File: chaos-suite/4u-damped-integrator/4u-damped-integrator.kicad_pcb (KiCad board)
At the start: 2 copper layers, 0 parts

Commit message: Laying out damped integrator pcb
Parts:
- added C1: 100pF, Rumblesan_Footprints:C_Rect_L7.0mm_W3.5mm_P5.00mm, F.Cu at (97.9, 111.0)
- added C10: 100nF, Rumblesan_Footprints:C_Rect_L7.0mm_W3.5mm_P5.00mm, F.Cu at (122.0, 100.6)
- added C11: 1uF, Capacitor_THT:CP_Radial_D5.0mm_P2.00mm, F.Cu at (102.6, 46.7)
- added C12: 1uF, Capacitor_THT:CP_Radial_D5.0mm_P2.00mm, F.Cu at (113.6, 46.7)
- added C2: 1nF, Rumblesan_Footprints:C_Rect_L7.0mm_W3.5mm_P5.00mm, F.Cu at (102.9, 86.6)
- added C3: 100pF, Rumblesan_Footprints:C_Rect_L7.0mm_W3.5mm_P5.00mm, F.Cu at (122.1, 111.0)
- added C4: 1nF, Rumblesan_Footprints:C_Rect_L7.0mm_W3.5mm_P5.00mm, F.Cu at (117.1, 86.6)
- added C5: 100nF, Rumblesan_Footprints:C_Rect_L7.0mm_W3.5mm_P5.00mm, F.Cu at (106.2, 164.6)
- added C6: 100nF, Rumblesan_Footprints:C_Rect_L7.0mm_W3.5mm_P5.00mm, F.Cu at (113.8, 145.1)
- added C7: 100nF, Rumblesan_Footprints:C_Rect_L7.0mm_W3.5mm_P5.00mm, F.Cu at (103.0, 66.0)
- added C8: 100nF, Rumblesan_Footprints:C_Rect_L7.0mm_W3.5mm_P5.00mm, F.Cu at (122.0, 66.0)
- added C9: 100nF, Rumblesan_Footprints:C_Rect_L7.0mm_W3.5mm_P5.00mm, F.Cu at (102.9, 100.6)
- added D1: 1N5818, Rumblesan_Footprints:D_DO-41_SOD81_P10.16mm_Horizontal, F.Cu at (98.0, 46.7)
- added D2: 1N5818, Rumblesan_Footprints:Diode_THT_P10.16mm_Horizontal, F.Cu at (120.1, 36.6)
- added D3: 4v3, Rumblesan_Footprints:D_DO-41_SOD81_P10.16mm_Horizontal, F.Cu at (121.7, 158.0)
- added D4: 4v3, Rumblesan_Footprints:D_DO-41_SOD81_P10.16mm_Horizontal, F.Cu at (121.7, 155.2)
- added H1: MountingHole_Pad, MountingHole:MountingHole_3.2mm_M3_DIN965_Pad, F.Cu at (39.5, 176.5)
- added H10: MouseBite, Panelization:mouse-bite-2mm-slot, F.Cu at (85.0, 75.0)
- added H2: MountingHole_Pad, MountingHole:MountingHole_3.2mm_M3_DIN965_Pad, F.Cu at (80.5, 33.5)
- added H3: MountingHole_Pad, MountingHole:MountingHole_3.2mm_M3_DIN965_Pad, F.Cu at (89.5, 176.5)
- added H4: MountingHole_Pad, MountingHole:MountingHole_3.2mm_M3_DIN965_Pad, F.Cu at (130.5, 33.5)
- added H5: MouseBite, Panelization:mouse-bite-2mm-slot, F.Cu at (85.0, 142.5)
- added H6: MouseBite, Panelization:mouse-bite-2mm-slot, F.Cu at (85.0, 165.0)
- added H7: MouseBite, Panelization:mouse-bite-2mm-slot, F.Cu at (85.0, 120.0)
- added H8: MouseBite, Panelization:mouse-bite-2mm-slot, F.Cu at (85.0, 97.5)
- added H9: MouseBite, Panelization:mouse-bite-2mm-slot, F.Cu at (85.0, 52.5)
- added J1: BananaJack_PanelMount, Rumblesan_Footprints:BananaJack_THT_JohnsonCinch_108-09, B.Cu at (47.3, 75.7)
- added J10: BananaJack_PanelMount, Rumblesan_Footprints:BananaJack_THT_JohnsonCinch_108-09, B.Cu at (72.7, 56.6)
- added J11: BananaJack_PanelMount, Rumblesan_Footprints:BananaJack_THT_JohnsonCinch_108-09, B.Cu at (72.7, 94.8)
- added J12: I2_IO_Ctrl, Connector_PinSocket_2.54mm:PinSocket_1x04_P2.54mm_Vertical, F.Cu at (81.5, 59.0)
- added J13: I2_IO_Main, Connector_PinHeader_2.54mm:PinHeader_1x04_P2.54mm_Vertical, B.Cu at (131.5, 59.0)
- added J14: I2_Damping_Ctrl, Connector_PinSocket_2.54mm:PinSocket_1x02_P2.54mm_Vertical, F.Cu at (81.5, 125.0)
- added J15: I2_Damping_Main, Connector_PinHeader_2.54mm:PinHeader_1x02_P2.54mm_Vertical, B.Cu at (131.5, 125.0)
- added J16: BananaJack_PanelMount, Rumblesan_Footprints:BananaJack_THT_JohnsonCinch_108-09, B.Cu at (72.7, 37.6)
- added J17: 4U_Power, Rumblesan_Footprints:4u_Power_Molex_KK-254_P2.54mm, F.Cu at (105.2, 36.6)
- added J18: BananaJack_PanelMount, Rumblesan_Footprints:BananaJack_THT_JohnsonCinch_108-09, B.Cu at (47.3, 170.9)
- added J19: BananaJack_PanelMount, Rumblesan_Footprints:BananaJack_THT_JohnsonCinch_108-09, B.Cu at (47.3, 151.9)
- added J2: BananaJack_PanelMount, Rumblesan_Footprints:BananaJack_THT_JohnsonCinch_108-09, B.Cu at (47.3, 56.6)
- added J20: BananaJack_PanelMount, Rumblesan_Footprints:BananaJack_THT_JohnsonCinch_108-09, B.Cu at (72.7, 151.9)
- added J21: BananaJack_PanelMount, Rumblesan_Footprints:BananaJack_THT_JohnsonCinch_108-09, B.Cu at (72.7, 170.9)
- added J22: Extras_Ctrl, Connector_PinSocket_2.54mm:PinSocket_1x04_P2.54mm_Vertical, F.Cu at (57.0, 177.0)
- added J23: Extras_Main, Connector_PinHeader_2.54mm:PinHeader_1x04_P2.54mm_Vertical, B.Cu at (107.0, 177.0)
- added J3: BananaJack_PanelMount, Rumblesan_Footprints:BananaJack_THT_JohnsonCinch_108-09, B.Cu at (47.3, 94.8)
- added J4: I1_IO_Ctrl, Connector_PinSocket_2.54mm:PinSocket_1x04_P2.54mm_Vertical, F.Cu at (38.5, 59.0)
- added J5: I1_IO_Main, Connector_PinHeader_2.54mm:PinHeader_1x04_P2.54mm_Vertical, B.Cu at (88.5, 59.0)
- added J6: I1_Damping_Ctrl, Connector_PinSocket_2.54mm:PinSocket_1x04_P2.54mm_Vertical, F.Cu at (38.5, 127.5)
- added J7: I1_Damping_Main, Connector_PinHeader_2.54mm:PinHeader_1x04_P2.54mm_Vertical, B.Cu at (88.5, 127.5)
- added J8: BananaJack_PanelMount, Rumblesan_Footprints:BananaJack_THT_JohnsonCinch_108-09, B.Cu at (47.3, 37.6)
- added J9: BananaJack_PanelMount, Rumblesan_Footprints:BananaJack_THT_JohnsonCinch_108-09, B.Cu at (72.7, 75.7)
- added Q1: 2N3904, Package_TO_SOT_THT:TO-92_Inline_Wide, F.Cu at (99.6, 118.0)
- added Q2: 2N3906, Package_TO_SOT_THT:TO-92_Inline_Wide, F.Cu at (96.0, 120.4)
- added Q3: 2N3904, Package_TO_SOT_THT:TO-92_Inline_Wide, F.Cu at (117.9, 116.8)
- added Q4: 2N3906, Package_TO_SOT_THT:TO-92_Inline_Wide, F.Cu at (123.4, 119.6)
- added R1: 270k, Rumblesan_Footprints:Resistor_THT_L6.3mm_D2.5mm_P10.16mm_Horizontal, F.Cu at (102.9, 97.0)
- added R10: 10k, Rumblesan_Footprints:Resistor_THT_L6.3mm_D2.5mm_P10.16mm_Horizontal, F.Cu at (89.9, 113.5)
- added R11: 270k, Rumblesan_Footprints:Resistor_THT_L6.3mm_D2.5mm_P10.16mm_Horizontal, F.Cu at (108.5, 90.9)
- added R12: 100k, Rumblesan_Footprints:Resistor_THT_L6.3mm_D2.5mm_P10.16mm_Horizontal, F.Cu at (127.3, 73.2)
- added R13: 100k, Rumblesan_Footprints:Resistor_THT_L6.3mm_D2.5mm_P10.16mm_Horizontal, F.Cu at (127.3, 76.2)
- added R14: 100k, Rumblesan_Footprints:Resistor_THT_L6.3mm_D2.5mm_P10.16mm_Horizontal, F.Cu at (127.3, 104.1)
- added R15: 220r, Rumblesan_Footprints:Resistor_THT_L6.3mm_D2.5mm_P10.16mm_Horizontal, F.Cu at (127.3, 70.1)
- added R16: 100k, Rumblesan_Footprints:Resistor_THT_L6.3mm_D2.5mm_P10.16mm_Horizontal, F.Cu at (127.3, 97.0)
- added R17: 220r, Rumblesan_Footprints:Resistor_THT_L6.3mm_D2.5mm_P10.16mm_Horizontal, F.Cu at (127.3, 79.2)
- added R18: 2k, Rumblesan_Footprints:Resistor_THT_L6.3mm_D2.5mm_P10.16mm_Horizontal, F.Cu at (127.3, 107.2)
- added R19: 100k, Rumblesan_Footprints:Resistor_THT_L6.3mm_D2.5mm_P10.16mm_Horizontal, F.Cu at (121.9, 126.0)
- added R2: 100k, Rumblesan_Footprints:Resistor_THT_L6.3mm_D2.5mm_P10.16mm_Horizontal, F.Cu at (92.7, 73.2)
- added R20: 10k, Rumblesan_Footprints:Resistor_THT_L6.3mm_D2.5mm_P10.16mm_Horizontal, F.Cu at (130.0, 113.5)
- added R21: 10k, Rumblesan_Footprints:Resistor_THT_L6.3mm_D2.5mm_P10.16mm_Horizontal, F.Cu at (99.3, 163.1)
- added R22: 10k, Rumblesan_Footprints:Resistor_THT_L6.3mm_D2.5mm_P10.16mm_Horizontal, F.Cu at (102.4, 152.9)
- added R23: 390k, Rumblesan_Footprints:Resistor_THT_L6.3mm_D2.5mm_P10.16mm_Horizontal, F.Cu at (117.9, 157.7)
- added R24: 2k2, Rumblesan_Footprints:Resistor_THT_L6.3mm_D2.5mm_P10.16mm_Horizontal, F.Cu at (128.5, 144.3)
- added R25: 27k, Rumblesan_Footprints:Resistor_THT_L6.3mm_D2.5mm_P10.16mm_Horizontal, F.Cu at (125.2, 144.3)
- added R26: 100k, Rumblesan_Footprints:Resistor_THT_L6.3mm_D2.5mm_P10.16mm_Horizontal, F.Cu at (117.9, 155.4)
- added R27: 100k, Rumblesan_Footprints:Resistor_THT_L6.3mm_D2.5mm_P10.16mm_Horizontal, F.Cu at (125.2, 156.7)
- added R3: 100k, Rumblesan_Footprints:Resistor_THT_L6.3mm_D2.5mm_P10.16mm_Horizontal, F.Cu at (92.7, 76.2)
- added R4: 100k, Rumblesan_Footprints:Resistor_THT_L6.3mm_D2.5mm_P10.16mm_Horizontal, F.Cu at (92.7, 104.1)
- added R5: 220r, Rumblesan_Footprints:Resistor_THT_L6.3mm_D2.5mm_P10.16mm_Horizontal, F.Cu at (92.7, 70.1)
- added R6: 100k, Rumblesan_Footprints:Resistor_THT_L6.3mm_D2.5mm_P10.16mm_Horizontal, F.Cu at (92.7, 94.0)
- added R7: 220r, Rumblesan_Footprints:Resistor_THT_L6.3mm_D2.5mm_P10.16mm_Horizontal, F.Cu at (92.7, 79.2)
- added R8: 2k, Rumblesan_Footprints:Resistor_THT_L6.3mm_D2.5mm_P10.16mm_Horizontal, F.Cu at (92.7, 107.2)
- added R9: 100k, Rumblesan_Footprints:Resistor_THT_L6.3mm_D2.5mm_P10.16mm_Horizontal, F.Cu at (101.6, 122.7)
- added RV1: 100k, Rumblesan_Footprints:Potentiometer_Alpha_RD901F-40-00D_Single_Vertical_CircularHoles, B.Cu at (47.3, 132.8)
- added RV2: 100k, Rumblesan_Footprints:Potentiometer_Alpha_RD901F-40-00D_Single_Vertical_CircularHoles, B.Cu at (47.3, 113.8)
- added RV3: 100k, Rumblesan_Footprints:Potentiometer_Alpha_RD901F-40-00D_Single_Vertical_CircularHoles, B.Cu at (72.7, 132.8)
- added RV4: 100k, Rumblesan_Footprints:Potentiometer_Alpha_RD901F-40-00D_Single_Vertical_CircularHoles, B.Cu at (72.7, 113.8)
- added U1: TL074, Rumblesan_Footprints:DIP-14_W7.62mm_Socket, F.Cu at (113.8, 109.5)
- added U2: LM13700, Rumblesan_Footprints:DIP-16_W7.62mm_Socket, F.Cu at (113.8, 79.8)
- added U3: TL072, Rumblesan_Footprints:DIP-8_W7.62mm_Socket, F.Cu at (113.8, 160.8)
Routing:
- net +12V: track 0.00 -> 214.5 mm
- net -12V: track 0.00 -> 122.2 mm
- net /I2_Output_Main: track 0.00 -> 48.7 mm
- net /I1_Output_Main: track 0.00 -> 48.0 mm
- net Net-(C1-Pad1): track 0.00 -> 43.4 mm
- net Net-(C3-Pad1): track 0.00 -> 35.4 mm
- net Net-(C2-Pad1): track 0.00 -> 34.7 mm
- net Net-(U2-Pad5): track 0.00 -> 34.7 mm
- net /Extras/Inverter_Output_Ctrl: track 0.00 -> 34.5 mm
- net /Extras/NonLinearity_Input_Ctrl: track 0.00 -> 33.8 mm
- net Net-(U2-Pad1): track 0.00 -> 32.4 mm
- net Net-(R10-Pad2): track 0.00 -> 32.3 mm
- net Net-(J11-Pad1): track 0.00 -> 31.9 mm
- net Net-(J3-Pad1): track 0.00 -> 31.9 mm
- net /I1_DampingCV_Main: track 0.00 -> 31.4 mm
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- added copper zone on B.Cu, net GND
- added copper zone on F.Cu, net GND
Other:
- board outline added: 98 x 150 mm
- net class Default removed
- net class Power removed
- net class Signal removed
- board text added: "Damped Integrator revision 01"
- board text added: "This side towards panel"

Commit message: final damped integrator tweaks
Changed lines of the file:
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@@
   (title_block
     (title "Damped Integrator and extras")
-    (date "2022-05-21")
+    (date "2022-06-17")
     (rev "r01")
+    (comment 2 "creativecommons.org/licenses/by/4.0/")
+    (comment 3 "License: CC BY 4.0")
+    (comment 4 "Author: Guy John")
   )
   (layers
@@
       (drillshape 0)
       (scaleselection 1)
-      (outputdirectory "")
+      (outputdirectory "pcb-gerbers/")
     )
   )
@@
   (net 58 "unconnected-(U2-Pad15)")
   (net 59 "unconnected-(U2-Pad8)")
-  (net 60 "Net-(U2-Pad5)")
+  (net 60 "Net-(C4-Pad1)")
   (net 61 "Net-(R2-Pad2)")
-  (net 62 "Net-(U2-Pad1)")
+  (net 62 "Net-(R20-Pad2)")
   (footprint "Rumblesan_Footprints:Resistor_THT_L6.3mm_D2.5mm_P10.16mm_Horizontal" (layer "F.Cu")
     (at 99.314 163.068 90)
@@
     (fp_line (start 1.635 -1.27) (end 6.985 -1.27) (layer "F.Fab") (width 0.1))
     (pad "1" thru_hole rect locked (at 0 0 180) (size 1.6 1.6) (drill 0.8) (layers *.Cu *.Mask)
-      (net 62 "Net-(U2-Pad1)") (pintype "input"))
+      (net 62 "Net-(R20-Pad2)") (pintype "input"))
     (pad "2" thru_hole oval locked (at 0 2.54 180) (size 1.6 1.6) (drill 0.8) (layers *.Cu *.Mask)
       (net 55 "unconnected-(U2-Pad2)") (pinfunction "DIODE_BIAS") (pintype "input+no_connect"))
@@
       (net 49 "Net-(R12-Pad2)") (pinfunction "-") (pintype "input"))
     (pad "5" thru_hole oval locked (at 0 10.16 180) (size 1.6 1.6) (drill 0.8) (layers *.Cu *.Mask)
-      (net 60 "Net-(U2-Pad5)") (pintype "output"))
+      (net 60 "Net-(C4-Pad1)") (pintype "output"))
     (pad "6" thru_hole oval locked (at 0 12.7 180) (size 1.6 1.6) (drill 0.8) (layers *.Cu *.Mask)
       (net 10 "-12V") (pinfunction "V-") (pintype "power_in"))
@@
     (fp_line (start -1.27 -0.5) (end -0.562893 0) (layer "F.Fab") (width 0.1))
     (fp_line (start 8.89 -2.92) (end -1.27 -2.92) (layer "F.Fab") (width 0.1))
-    (pad "1" thru_hole roundrect (at 0 0) (size 1.74 2.19) (drill 1.19) (layers *.Cu *.Mask) (roundrect_rratio 0.143678)
+    (pad "1" thru_hole roundrect (at 0 0) (size 1.74 2.19) (drill 1.19) (layers *.Cu *.Mask) (roundrect_rratio 0.1436781609)
       (net 11 "Net-(D1-Pad2)") (pinfunction "+12V") (pintype "power_out"))
     (pad "2" thru_hole oval (at 2.54 0) (size 1.74 2.19) (drill 1.19) (layers *.Cu *.Mask)
@@
       (net 46 "Net-(Q4-Pad3)") (pintype "passive"))
     (pad "2" thru_hole oval (at 10.16 0 90) (size 1.6 1.6) (drill 0.8) (layers *.Cu *.Mask)
-      (net 62 "Net-(U2-Pad1)") (pintype "passive"))
+      (net 62 "Net-(R20-Pad2)") (pintype "passive"))
     (model "${KISYS3DMOD}/Resistor_THT.3dshapes/R_Axial_DIN0207_L6.3mm_D2.5mm_P10.16mm_Horizontal.wrl"
       (offset (xyz 0 0 0))
@@
     (fp_line (start -1 1.75) (end 6 1.75) (layer "F.Fab") (width 0.1))
     (pad "1" thru_hole circle (at 0 0) (size 1.6 1.6) (drill 0.8) (layers *.Cu *.Mask)
-      (net 60 "Net-(U2-Pad5)") (pintype "passive"))
+      (net 60 "Net-(C4-Pad1)") (pintype "passive"))
     (pad "2" thru_hole circle (at 5 0) (size 1.6 1.6) (drill 0.8) (layers *.Cu *.Mask)
       (net 7 "/I2_Output_Main") (pintype "passive"))
@@
       (net 9 "GND") (pinfunction "+") (pintype "input"))
     (pad "6" thru_hole oval locked (at 0 12.7 180) (size 1.6 1.6) (drill 0.8) (layers *.Cu *.Mask)
-      (net 60 "Net-(U2-Pad5)") (pinfunction "-") (pintype "input"))
+      (net 60 "Net-(C4-Pad1)") (pinfunction "-") (pintype "input"))
     (pad "7" thru_hole oval locked (at 0 15.24 180) (size 1.6 1.6) (drill 0.8) (layers *.Cu *.Mask)
       (net 7 "/I2_Output_Main") (pintype "output"))

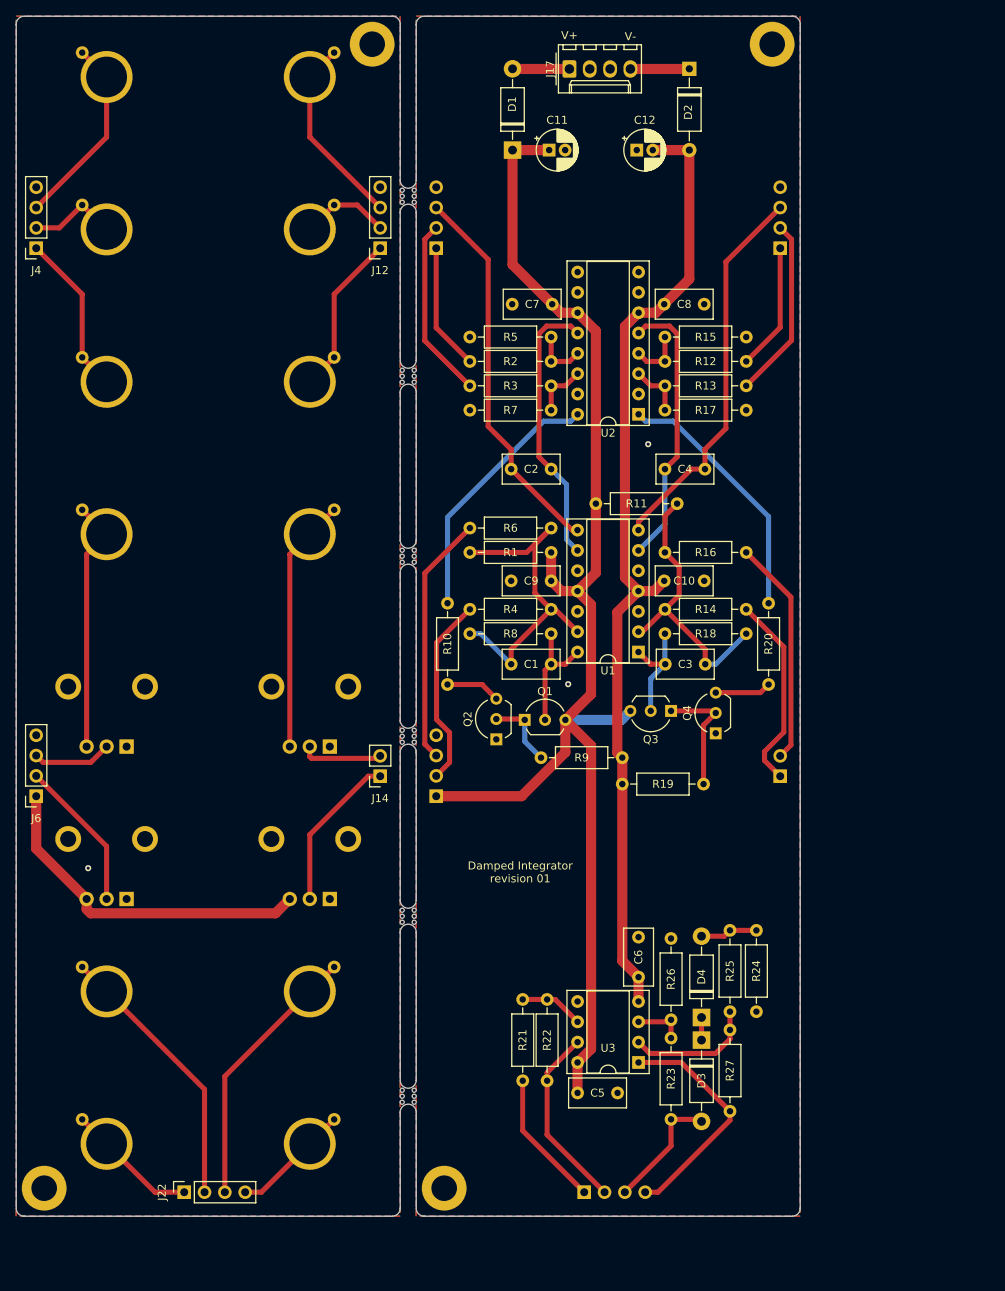
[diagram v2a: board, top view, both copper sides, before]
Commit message: Updating damped integrator circuit and layout
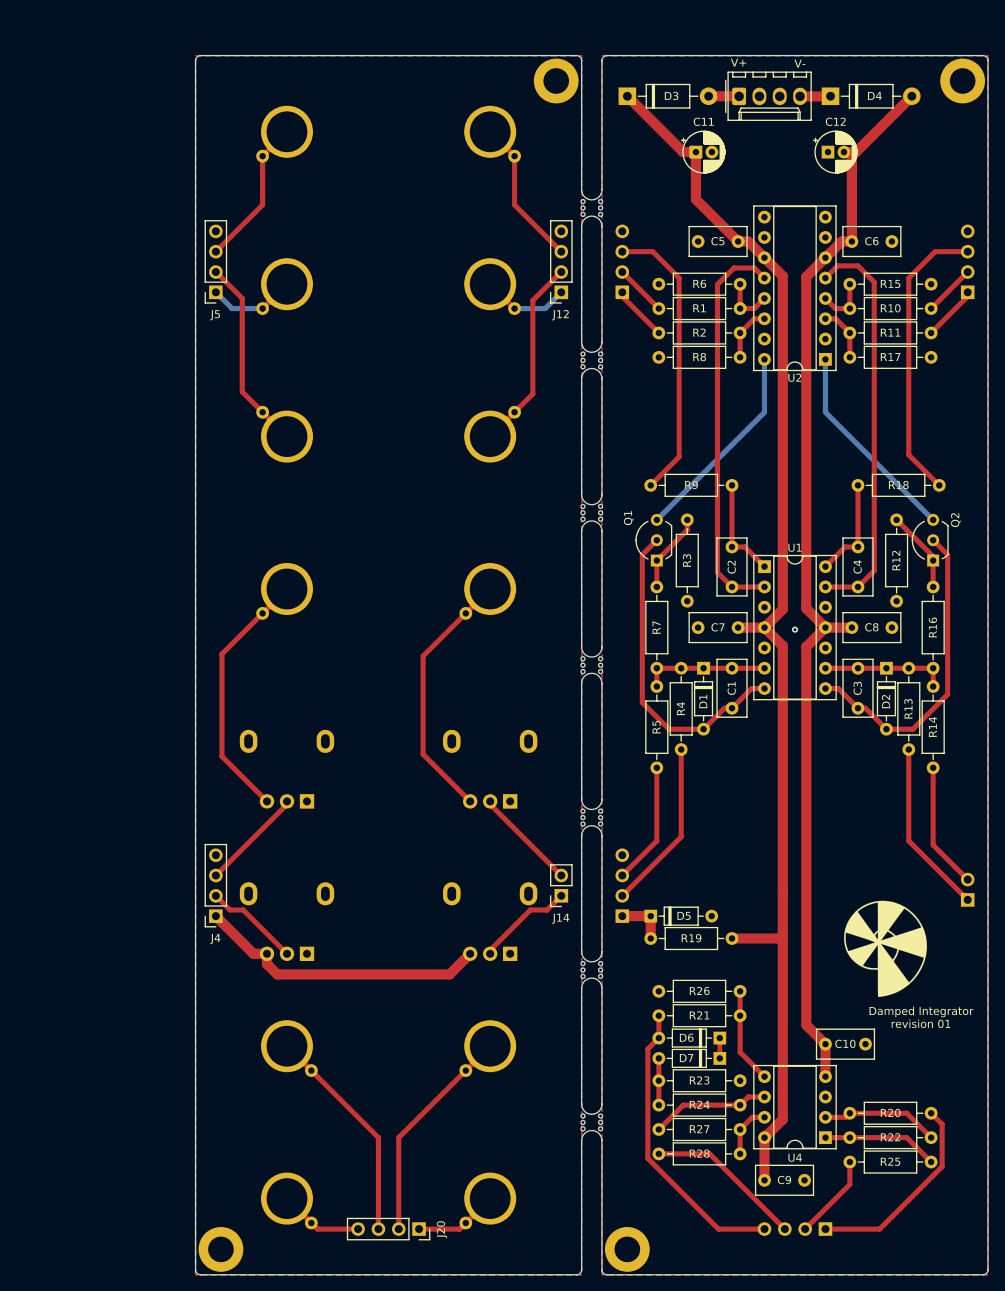
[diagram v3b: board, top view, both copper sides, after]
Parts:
- removed H10, H5, H6, H7, H8, H9: MouseBite, Panelization:mouse-bite-2mm-slot
- removed Q3: 2N3904, Package_TO_SOT_THT:TO-92_Inline_Wide
- removed Q4: 2N3906, Package_TO_SOT_THT:TO-92_Inline_Wide
- removed U3: TL072, Rumblesan_Footprints:DIP-8_W7.62mm_Socket
- added D5: 5v1, rumblesan-standard-parts:D_DO-35_SOD27_P7.62mm_Horizontal, F.Cu at (115.3, 142.5)
- added D6: 4v3, rumblesan-standard-parts:D_DO-35_SOD27_P7.62mm_Horizontal, F.Cu at (124.0, 157.7)
- added D7: 4v3, rumblesan-standard-parts:D_DO-35_SOD27_P7.62mm_Horizontal, F.Cu at (124.0, 160.3)
- added G***: LOGO, Rumblesan_Panel_Graphics:Logo_Ammonite-simple_small_10.4mmx12.0mm, F.Cu at (144.0, 145.5)
- added R28: 330r, rumblesan-standard-parts:R_Axial_DIN0207_L6.3mm_D2.5mm_P10.16mm_Horizontal, F.Cu at (116.3, 172.2)
- added U4: TL072, rumblesan-standard-parts:DIP-8_W7.62mm_Socket, F.Cu at (137.2, 170.2)
- added mouse-bite-2.54mm-slot: VAL**, Panelization:mouse-bite-2.54mm-slot, F.Cu at (108.0, 92.1)
- added mouse-bite-2.54mm-slot: VAL**, Panelization:mouse-bite-2.54mm-slot, F.Cu at (108.0, 73.0)
- added mouse-bite-2.54mm-slot: VAL**, Panelization:mouse-bite-2.54mm-slot, F.Cu at (108.0, 54.0)
- added mouse-bite-2.54mm-slot: VAL**, Panelization:mouse-bite-2.54mm-slot, F.Cu at (108.0, 130.2)
- added mouse-bite-2.54mm-slot: VAL**, Panelization:mouse-bite-2.54mm-slot, F.Cu at (108.0, 149.2)
- added mouse-bite-2.54mm-slot: VAL**, Panelization:mouse-bite-2.54mm-slot, F.Cu at (108.0, 111.1)
- added mouse-bite-2.54mm-slot: VAL**, Panelization:mouse-bite-2.54mm-slot, F.Cu at (108.0, 168.3)
- C1, C10, C2, C3, C4, C5, C6, C7, C8, C9: footprint Rumblesan_Footprints:C_Rect_L7.0mm_W3.5mm_P5.00mm -> rumblesan-standard-parts:C_Rect_L7.0mm_W3.5mm_P5.00mm
- C11, C12: footprint Capacitor_THT:CP_Radial_D5.0mm_P2.00mm -> rumblesan-standard-parts:CP_Radial_D5.0mm_P2.00mm
- D1: value 1N5818 -> 1n4148; footprint Rumblesan_Footprints:D_DO-41_SOD81_P10.16mm_Horizontal -> rumblesan-standard-parts:D_DO-35_SOD27_P7.62mm_Horizontal
- D2: value 1N5818 -> 1n4148; footprint Rumblesan_Footprints:Diode_THT_P10.16mm_Horizontal -> rumblesan-standard-parts:D_DO-35_SOD27_P7.62mm_Horizontal
- D3, D4: value 4v3 -> 1N5818; footprint Rumblesan_Footprints:D_DO-41_SOD81_P10.16mm_Horizontal -> rumblesan-standard-parts:D_DO-41_SOD81_P10.16mm_Horizontal
- H1, H2, H3, H4: footprint MountingHole:MountingHole_3.2mm_M3_DIN965_Pad -> rumblesan-standard-parts:MountingHole_3.2mm_M3_DIN965_Pad
- J1, J10, J11, J16, J18, J19, J2, J3, J8, J9: value BananaJack_PanelMount -> Banana Socket PanelMount; footprint Rumblesan_Footprints:BananaJack_THT_JohnsonCinch_108-09 -> rumblesan-standard-parts:BananaJack_THT_JohnsonCinch_108-09
- J12: value I2_IO_Ctrl -> Conn_01x04_Female
- J13: value I2_IO_Main -> Conn_01x04_Male
- J14: value I2_Damping_Ctrl -> Conn_01x02_Female
- J15: value I2_Damping_Main -> Conn_01x02_Male
- J17: footprint Rumblesan_Footprints:4u_Power_Molex_KK-254_P2.54mm -> 4u-power:4u_Power_Molex_KK-254_P2.54mm
- J20: value BananaJack_PanelMount -> Conn_01x04_Female; footprint Rumblesan_Footprints:BananaJack_THT_JohnsonCinch_108-09 -> Connector_PinSocket_2.54mm:PinSocket_1x04_P2.54mm_Vertical; moved to F.Cu
- J21: value BananaJack_PanelMount -> Conn_01x04_Male; footprint Rumblesan_Footprints:BananaJack_THT_JohnsonCinch_108-09 -> Connector_PinHeader_2.54mm:PinHeader_1x04_P2.54mm_Vertical
- J22: value Extras_Ctrl -> Banana Socket PanelMount; footprint Connector_PinSocket_2.54mm:PinSocket_1x04_P2.54mm_Vertical -> rumblesan-standard-parts:BananaJack_THT_JohnsonCinch_108-09; moved to B.Cu
- J23: value Extras_Main -> Banana Socket PanelMount; footprint Connector_PinHeader_2.54mm:PinHeader_1x04_P2.54mm_Vertical -> rumblesan-standard-parts:BananaJack_THT_JohnsonCinch_108-09
- J4: value I1_IO_Ctrl -> Conn_01x04_Female
- J5: value I1_IO_Main -> Conn_01x04_Female; footprint Connector_PinHeader_2.54mm:PinHeader_1x04_P2.54mm_Vertical -> Connector_PinSocket_2.54mm:PinSocket_1x04_P2.54mm_Vertical; moved to F.Cu
- J6: value I1_Damping_Ctrl -> Conn_01x04_Male; footprint Connector_PinSocket_2.54mm:PinSocket_1x04_P2.54mm_Vertical -> Connector_PinHeader_2.54mm:PinHeader_1x04_P2.54mm_Vertical; moved to B.Cu
- J7: value I1_Damping_Main -> Conn_01x04_Male
- Q1: value 2N3904 -> 2N3906
- R1, R11: value 270k -> 100k; footprint Rumblesan_Footprints:Resistor_THT_L6.3mm_D2.5mm_P10.16mm_Horizontal -> rumblesan-standard-parts:R_Axial_DIN0207_L6.3mm_D2.5mm_P10.16mm_Horizontal
- R10: value 10k -> 100k; footprint Rumblesan_Footprints:Resistor_THT_L6.3mm_D2.5mm_P10.16mm_Horizontal -> rumblesan-standard-parts:R_Axial_DIN0207_L6.3mm_D2.5mm_P10.16mm_Horizontal
- R12, R3: value 100k -> 10k; footprint Rumblesan_Footprints:Resistor_THT_L6.3mm_D2.5mm_P10.16mm_Horizontal -> rumblesan-standard-parts:R_Axial_DIN0207_L6.3mm_D2.5mm_P10.16mm_Horizontal
- R13, R14, R15, R16, R17, R2, R20, R22, R26, R27, R4: footprint Rumblesan_Footprints:Resistor_THT_L6.3mm_D2.5mm_P10.16mm_Horizontal -> rumblesan-standard-parts:R_Axial_DIN0207_L6.3mm_D2.5mm_P10.16mm_Horizontal
- R18: value 2k -> 330r; footprint Rumblesan_Footprints:Resistor_THT_L6.3mm_D2.5mm_P10.16mm_Horizontal -> rumblesan-standard-parts:R_Axial_DIN0207_L6.3mm_D2.5mm_P10.16mm_Horizontal
- R19: value 100k -> 1k; footprint Rumblesan_Footprints:Resistor_THT_L6.3mm_D2.5mm_P10.16mm_Horizontal -> rumblesan-standard-parts:R_Axial_DIN0207_L6.3mm_D2.5mm_P10.16mm_Horizontal
- R21: value 10k -> 390k; footprint Rumblesan_Footprints:Resistor_THT_L6.3mm_D2.5mm_P10.16mm_Horizontal -> rumblesan-standard-parts:R_Axial_DIN0207_L6.3mm_D2.5mm_P10.16mm_Horizontal
- R23: value 390k -> 2k2; footprint Rumblesan_Footprints:Resistor_THT_L6.3mm_D2.5mm_P10.16mm_Horizontal -> rumblesan-standard-parts:R_Axial_DIN0207_L6.3mm_D2.5mm_P10.16mm_Horizontal
- R24: value 2k2 -> 27k; footprint Rumblesan_Footprints:Resistor_THT_L6.3mm_D2.5mm_P10.16mm_Horizontal -> rumblesan-standard-parts:R_Axial_DIN0207_L6.3mm_D2.5mm_P10.16mm_Horizontal
- R25: value 27k -> 330r; footprint Rumblesan_Footprints:Resistor_THT_L6.3mm_D2.5mm_P10.16mm_Horizontal -> rumblesan-standard-parts:R_Axial_DIN0207_L6.3mm_D2.5mm_P10.16mm_Horizontal
- R5, R7: value 220r -> 100k; footprint Rumblesan_Footprints:Resistor_THT_L6.3mm_D2.5mm_P10.16mm_Horizontal -> rumblesan-standard-parts:R_Axial_DIN0207_L6.3mm_D2.5mm_P10.16mm_Horizontal
- R6: value 100k -> 220r; footprint Rumblesan_Footprints:Resistor_THT_L6.3mm_D2.5mm_P10.16mm_Horizontal -> rumblesan-standard-parts:R_Axial_DIN0207_L6.3mm_D2.5mm_P10.16mm_Horizontal
- R8: value 2k -> 220r; footprint Rumblesan_Footprints:Resistor_THT_L6.3mm_D2.5mm_P10.16mm_Horizontal -> rumblesan-standard-parts:R_Axial_DIN0207_L6.3mm_D2.5mm_P10.16mm_Horizontal
- R9: value 100k -> 330r; footprint Rumblesan_Footprints:Resistor_THT_L6.3mm_D2.5mm_P10.16mm_Horizontal -> rumblesan-standard-parts:R_Axial_DIN0207_L6.3mm_D2.5mm_P10.16mm_Horizontal
- RV1, RV2, RV3, RV4: footprint Rumblesan_Footprints:Potentiometer_Alpha_RD901F-40-00D_Single_Vertical_CircularHoles -> rumblesan-standard-parts:Potentiometer_Alpha_RD901F-40-00D_Single_Vertical
- U1: footprint Rumblesan_Footprints:DIP-14_W7.62mm_Socket -> rumblesan-standard-parts:DIP-14_W7.62mm_Socket
- U2: footprint Rumblesan_Footprints:DIP-16_W7.62mm_Socket -> rumblesan-standard-parts:DIP-16_W7.62mm_Socket
- moved D3 118.3 mm to (112.4, 40.0), turned to 0 degrees
- moved D4 116.3 mm to (137.8, 40.0), turned to 0 degrees
- moved C5 108.3 mm to (126.2, 58.2), turned to 180 degrees
- moved C6 92.5 mm to (145.5, 58.2), turned to 180 degrees
- moved J4 86.5 mm to (61.0, 142.5)
- moved C9 79.5 mm to (129.5, 175.5), turned to 0 degrees
- moved D2 78.9 mm to (144.8, 111.5)
- moved J6 74.8 mm to (111.8, 142.5), turned to 0 degrees
- moved D1 69.0 mm to (121.9, 111.5), turned to -90 degrees
- moved R10 68.8 mm to (140.2, 66.5), turned to 0 degrees
- moved J7 67.1 mm to (111.8, 64.5)
- moved J21 65.3 mm to (137.2, 181.6)
- moved C10 61.3 mm to (142.2, 158.5)
- moved Q2 59.0 mm to (150.6, 98.0)
- moved R5 58.7 mm to (116.1, 124.0), turned to 90 degrees
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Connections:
- C2 pad 2: /I1_Output_Main -> Net-(C2-Pad2)
- C4 pad 2: /I2_Output_Main -> Net-(C4-Pad2)
- D1 pad 1: +12V -> Net-(C1-Pad1)
- D1 pad 2: Net-(D1-Pad2) -> Net-(C1-Pad2)
- D2 pad 1: Net-(D2-Pad1) -> Net-(C3-Pad1)
- D2 pad 2: -12V -> Net-(C3-Pad2)
- D3 pad 1: Net-(D3-Pad1) -> +12V
- D3 pad 2: /Extras/NonLinearity_Input_Main -> Net-(D3-Pad2)
- D4 pad 1: Net-(D3-Pad1) -> Net-(D4-Pad1)
- D4 pad 2: Net-(D4-Pad2) -> -12V
- J10 pad 1: /I2_InputPos_Ctrl -> /I2_InputNeg_Ctrl
- J11 pad 1: Net-(J11-Pad1) -> /I2_InputPos_Ctrl
- J12 pad 1: /I2_InputNeg_Ctrl -> /I2_InputPos_Ctrl
- J12 pad 2: /I2_InputPos_Ctrl -> /I2_InputNeg_Ctrl
- J13 pad 1: /I2_InputNeg_Main -> /I2_InputPos_Main
- J13 pad 2: /I2_InputPos_Main -> /I2_InputNeg_Main
- J14 pad 1: /I2_Damping_Ctrl -> /I2_Rate_Ctrl
- J14 pad 2: /I2_DampingCV_Ctrl -> /I2_RateCV_Ctrl
- J15 pad 1: /I2_Damping_Main -> /I2_Rate_Main
- J15 pad 2: /I2_DampingCV_Main -> /I2_RateCV_Main
- J17 pad 1: Net-(D1-Pad2) -> Net-(D3-Pad2)
- J17 pad 4: Net-(D2-Pad1) -> Net-(D4-Pad1)
- J19 pad 1: /Extras/Inverter_Output_Ctrl -> /Extras/NonLinearity_Input_Ctrl
- J20 pad 1: /Extras/NonLinearity_Input_Ctrl -> /Extras/Inverter_Input_Ctrl
- J21 pad 1: /Extras/NonLinearity_Output_Ctrl -> /Extras/Inverter_Input_Main
- J22 pad 1: /Extras/Inverter_Input_Ctrl -> /Extras/Inverter_Output_Ctrl
- J23 pad 1: /Extras/Inverter_Input_Main -> /Extras/NonLinearity_Output_Ctrl
- J4 pad 1: /I1_InputNeg_Ctrl -> V_REF
- J4 pad 2: /I1_InputPos_Ctrl -> /I1_Rate_Ctrl
- J4 pad 3: /I1_Output_Ctrl -> /I1_RateCV_Ctrl
- J5 pad 1: /I1_InputNeg_Main -> /I1_InputPos_Ctrl
- J5 pad 2: /I1_InputPos_Main -> /I1_InputNeg_Ctrl
- J5 pad 3: /I1_Output_Main -> /I1_Output_Ctrl
- J6 pad 1: +12V -> V_REF
- J6 pad 2: /I1_Damping_Ctrl -> /I1_Rate_Main
- J6 pad 3: /I1_DampingCV_Ctrl -> /I1_RateCV_Main
- J7 pad 1: +12V -> /I1_InputPos_Main
- J7 pad 2: /I1_Damping_Main -> /I1_InputNeg_Main
- J7 pad 3: /I1_DampingCV_Main -> /I1_Output_Main
- J9 pad 1: /I2_InputNeg_Ctrl -> Net-(J9-Pad1)
- Q1 pad 3: +12V -> Net-(Q1-Pad3)
- Q2 pad 1: GND -> Net-(Q2-Pad1)
- Q2 pad 2: Net-(Q1-Pad1) -> Net-(C3-Pad2)
- R1 pad 1: +12V -> Net-(R1-Pad1)
- R1 pad 2: Net-(C1-Pad1) -> /I1_InputNeg_Main
- R10 pad 1: Net-(Q2-Pad3) -> Net-(R10-Pad1)
- R10 pad 2: Net-(R10-Pad2) -> /I2_InputNeg_Main
- R11 pad 1: +12V -> Net-(R11-Pad1)
- R11 pad 2: Net-(C3-Pad1) -> /I2_InputPos_Main
- R12 pad 1: /I2_InputNeg_Main -> GND
- R12 pad 2: Net-(R12-Pad2) -> Net-(Q2-Pad1)
- R13 pad 1: /I2_InputPos_Main -> Net-(C3-Pad1)
- R13 pad 2: Net-(R13-Pad2) -> /I2_Rate_Main
- R14 pad 1: /I2_Damping_Main -> /I2_RateCV_Main
- R15 pad 1: GND -> Net-(R10-Pad1)
- R15 pad 2: Net-(R12-Pad2) -> GND
- R16 pad 1: /I2_DampingCV_Main -> Net-(Q2-Pad1)
- R17 pad 1: GND -> Net-(R11-Pad1)
- R17 pad 2: Net-(R13-Pad2) -> GND
- R18 pad 1: Net-(C3-Pad1) -> /I2_Output_Main
- R18 pad 2: Net-(C3-Pad2) -> Net-(C4-Pad2)
- R19 pad 1: Net-(Q3-Pad1) -> V_REF
- R19 pad 2: -12V -> +12V
- R2 pad 1: /I1_InputNeg_Main -> Net-(R2-Pad1)
- R2 pad 2: Net-(R2-Pad2) -> /I1_InputPos_Main
- R20 pad 1: Net-(Q4-Pad3) -> Net-(R20-Pad1)
- R20 pad 2: Net-(R20-Pad2) -> /Extras/Inverter_Input_Main
- R21 pad 1: /Extras/Inverter_Input_Main -> /Extras/NonLinearity_Input_Main
- R22 pad 1: Net-(R21-Pad2) -> Net-(R22-Pad1)
- R22 pad 2: /Extras/Inverter_Output_Main -> Net-(R20-Pad1)
- R23 pad 1: Net-(R23-Pad1) -> GND
- R23 pad 2: /Extras/NonLinearity_Input_Main -> Net-(D7-Pad2)
- R24 pad 1: Net-(D4-Pad2) -> Net-(R24-Pad1)
- R24 pad 2: GND -> Net-(D7-Pad2)
- R25 pad 1: Net-(D4-Pad2) -> /Extras/Inverter_Output_Main
- R25 pad 2: Net-(R25-Pad2) -> Net-(R22-Pad1)
- R26 pad 1: Net-(R23-Pad1) -> GND
- R26 pad 2: GND -> Net-(R21-Pad2)
- R27 pad 1: Net-(R25-Pad2) -> Net-(R27-Pad1)
- R27 pad 2: /Extras/NonLinearity_Output_Main -> Net-(R24-Pad1)
- R3 pad 1: /I1_InputPos_Main -> GND
- R3 pad 2: Net-(R3-Pad2) -> Net-(Q1-Pad1)
- R4 pad 1: /I1_Damping_Main -> Net-(C1-Pad1)
- R4 pad 2: Net-(C1-Pad1) -> /I1_Rate_Main
- R5 pad 1: GND -> /I1_RateCV_Main
- R5 pad 2: Net-(R2-Pad2) -> Net-(C1-Pad1)
- R6 pad 1: /I1_DampingCV_Main -> Net-(R1-Pad1)
- R6 pad 2: Net-(C1-Pad1) -> GND
- R7 pad 1: GND -> Net-(Q1-Pad1)
- R7 pad 2: Net-(R3-Pad2) -> Net-(C1-Pad1)
- R8 pad 1: Net-(C1-Pad1) -> Net-(R2-Pad1)
- R8 pad 2: Net-(C1-Pad2) -> GND
- R9 pad 1: Net-(Q1-Pad1) -> /I1_Output_Main
- R9 pad 2: -12V -> Net-(C2-Pad2)
- RV1 pad 2: /I1_Damping_Ctrl -> /I1_RateCV_Ctrl
- RV1 pad 3: +12V -> Net-(J3-Pad1)
- RV2 pad 2: /I1_DampingCV_Ctrl -> /I1_Rate_Ctrl
- RV2 pad 3: Net-(J3-Pad1) -> V_REF
- RV3 pad 2: /I2_Damping_Ctrl -> /I2_RateCV_Ctrl
- RV3 pad 3: +12V -> Net-(J9-Pad1)
- RV4 pad 2: /I2_DampingCV_Ctrl -> /I2_Rate_Ctrl
- RV4 pad 3: Net-(J11-Pad1) -> V_REF
- U1 pad 1: Net-(C3-Pad2) -> Net-(C2-Pad2)
- U1 pad 11: +12V -> -12V
- U1 pad 13: Net-(C1-Pad1) -> Net-(C4-Pad1)
- U1 pad 14: Net-(C1-Pad2) -> Net-(C4-Pad2)
- U1 pad 2: Net-(C3-Pad1) -> Net-(C2-Pad1)
- U1 pad 4: -12V -> +12V
- U1 pad 6: Net-(C4-Pad1) -> Net-(C1-Pad1)
- U1 pad 7: /I2_Output_Main -> Net-(C1-Pad2)
- U1 pad 8: /I1_Output_Main -> Net-(C3-Pad2)
- U1 pad 9: Net-(C2-Pad1) -> Net-(C3-Pad1)
- U2 pad 1: Net-(R20-Pad2) -> Net-(Q2-Pad3)
- U2 pad 13: Net-(R2-Pad2) -> Net-(R1-Pad1)
- U2 pad 14: Net-(R3-Pad2) -> Net-(R2-Pad1)
- U2 pad 16: Net-(R10-Pad2) -> Net-(Q1-Pad3)
- U2 pad 3: Net-(R13-Pad2) -> Net-(R11-Pad1)
- U2 pad 4: Net-(R12-Pad2) -> Net-(R10-Pad1)
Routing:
- net +12V: track 214.5 -> 157.8 mm
- net V_REF: track 0.00 -> 43.0 mm
- net Net-(J9-Pad1): track 0.00 -> 32.5 mm
- net Net-(R20-Pad2): track 32.4 -> 0.00 mm
- net Net-(R10-Pad2): track 32.3 -> 0.00 mm
- net Net-(J11-Pad1): track 31.9 -> 0.00 mm
- net /I1_DampingCV_Main: track 31.4 -> 0.00 mm
- net /I2_DampingCV_Main: track 28.3 -> 0.00 mm
- net Net-(C1-Pad1): track 43.4 -> 15.7 mm
- net Net-(Q1-Pad3): track 0.00 -> 25.6 mm
- net Net-(C3-Pad2): track 14.3 -> 39.2 mm
- net Net-(C1-Pad2): track 15.0 -> 39.8 mm
- net /I2_Damping_Main: track 24.6 -> 0.00 mm
- net /I1_Damping_Main: track 23.9 -> 0.00 mm
- net /Extras/NonLinearity_Input_Ctrl: track 33.8 -> 10.5 mm
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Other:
- board size 98 x 150 mm -> 99.1 x 152.4 mm
